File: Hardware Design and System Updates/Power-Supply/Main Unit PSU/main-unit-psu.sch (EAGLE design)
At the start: 12 parts, among them U1 BA033CC0FP-E2TO252-3_ROM, U2 BA033CC0FP-E2TO252-3_ROM

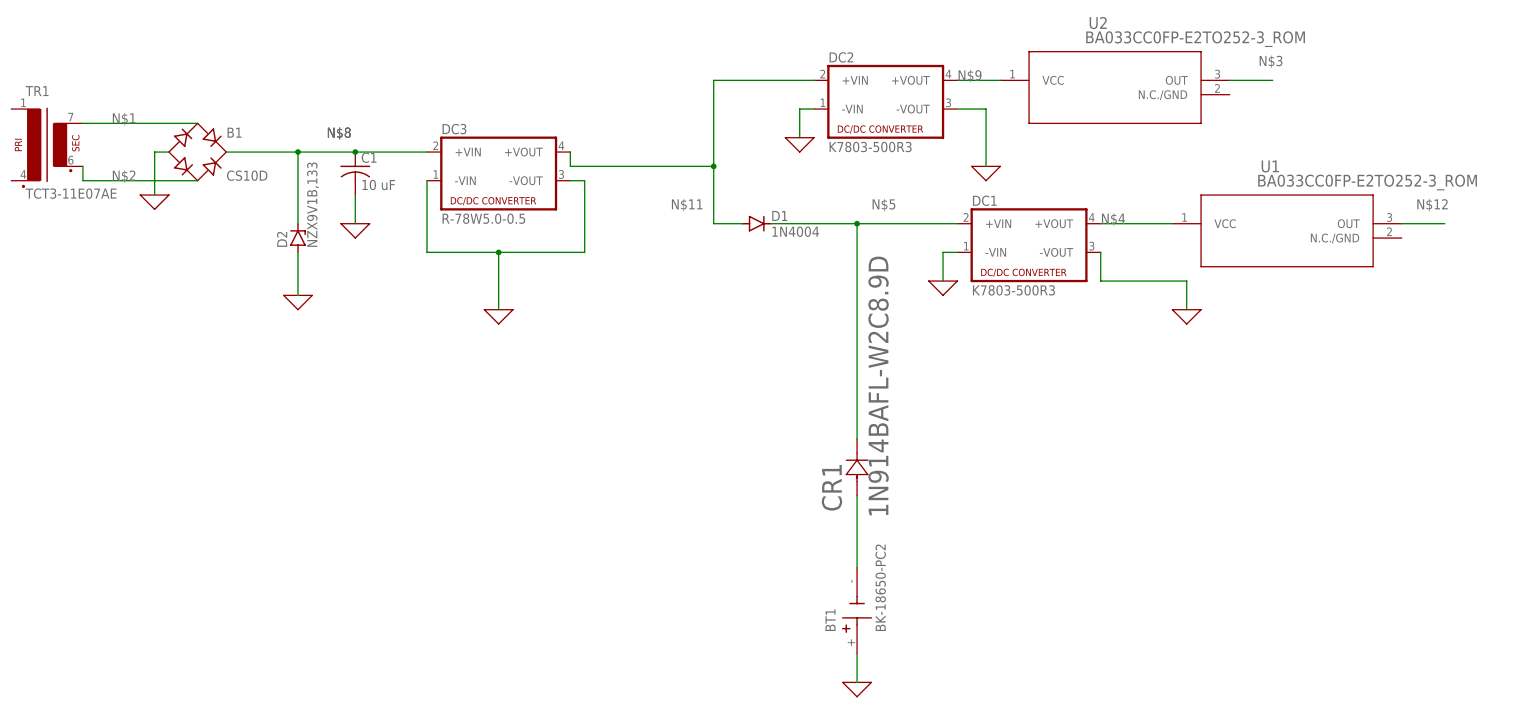
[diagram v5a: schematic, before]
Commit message: Fixed main and sub unit designs for voltage compat
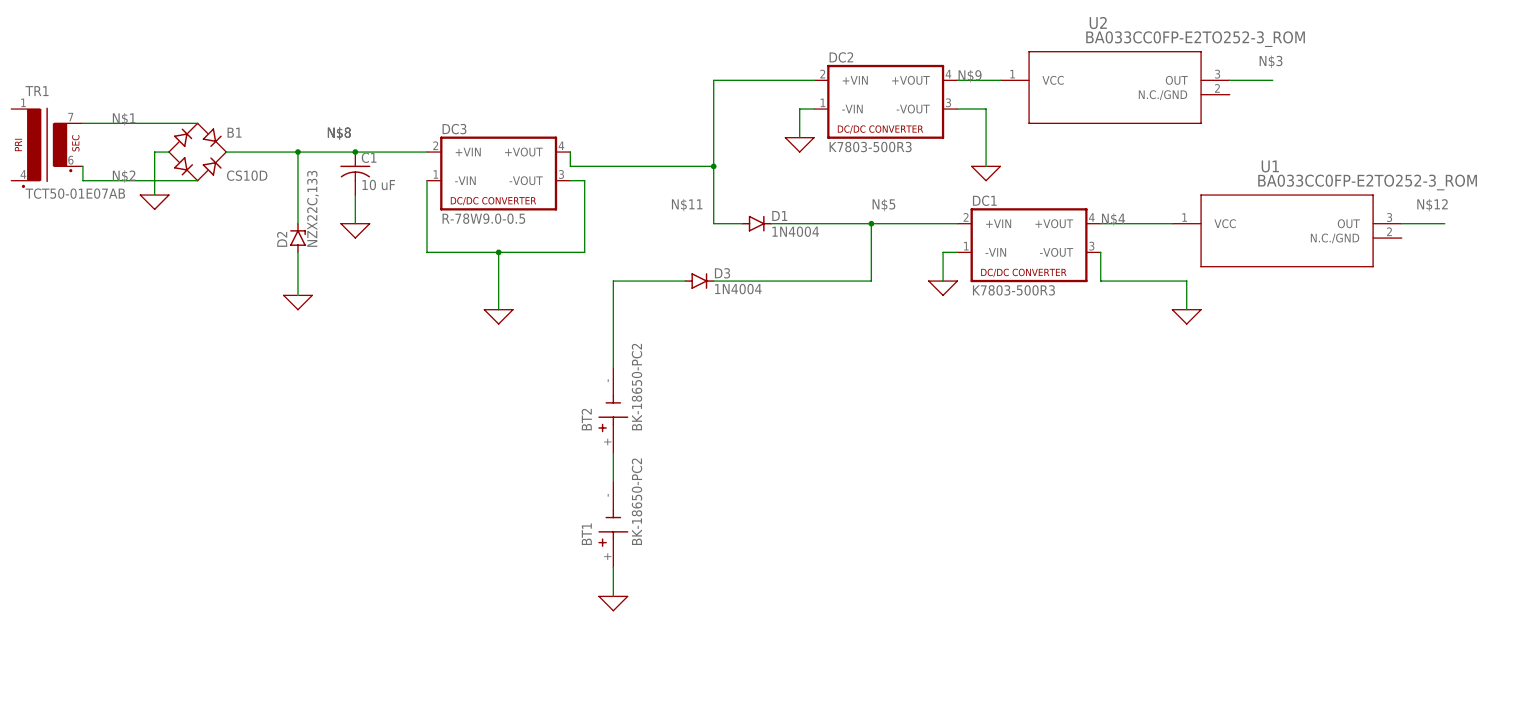
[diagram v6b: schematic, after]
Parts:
- removed CR1: 1N914BAFL-W2C8.9D, 2023-03-08_11-41-24_Library:1N914BAFL-W2C8.9D
- added BT2: BK-18650-PC2, BK-18650-PC2:BK-18650-PC2
- added D3: 1N4004, diode:1N4004
- D2: value NZX9V1B,133 -> NZX22C,133
- DC3: value R-78W5.0-0.5 -> R-78W9.0-0.5
- TR1: value TCT3-11E07AE -> TCT50-01E07AB
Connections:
- new net N$7: BT2.-, D3.A
- net N$5: now also D3.C; no longer CR1.1
- net N$6: now also BT2.+; no longer CR1.2
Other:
- moved on the sheet: BT1
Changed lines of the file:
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@@
 <part name="B1" library="rectifier" library_urn="urn:adsk.eagle:library:336" deviceset="B-DIL" device="" package3d_urn="urn:adsk.eagle:package:23868/1" value="CS10D"/>
 <part name="X_1" library="ngspice-simulation" library_urn="urn:adsk.eagle:library:527439" deviceset="GND" device=""/>
-<part name="D2" library="diode" library_urn="urn:adsk.eagle:library:210" deviceset="ZENER-DIODE" device="DO41Z10" package3d_urn="urn:adsk.eagle:package:43341/1" value="NZX9V1B,133"/>
+<part name="D2" library="diode" library_urn="urn:adsk.eagle:library:210" deviceset="ZENER-DIODE" device="DO41Z10" package3d_urn="urn:adsk.eagle:package:43341/1" value="NZX22C,133"/>
 <part name="X_2" library="ngspice-simulation" library_urn="urn:adsk.eagle:library:527439" deviceset="GND" device=""/>
 <part name="X_3" library="ngspice-simulation" library_urn="urn:adsk.eagle:library:527439" deviceset="GND" device=""/>
-<part name="TR1" library="trafo" library_urn="urn:adsk.eagle:library:394" deviceset="EE20-1" device="" package3d_urn="urn:adsk.eagle:package:28342/1" value="TCT3-11E07AE"/>
+<part name="TR1" library="trafo" library_urn="urn:adsk.eagle:library:394" deviceset="EE20-1" device="" package3d_urn="urn:adsk.eagle:package:28342/1" value="TCT50-01E07AB"/>
 <part name="DC1" library="dc-dc-converter" library_urn="urn:adsk.eagle:library:208" deviceset="NME" device="" package3d_urn="urn:adsk.eagle:package:12313/1" value="K7803-500R3"/>
 <part name="X_4" library="ngspice-simulation" library_urn="urn:adsk.eagle:library:527439" deviceset="GND" device=""/>
 <part name="DC2" library="dc-dc-converter" library_urn="urn:adsk.eagle:library:208" deviceset="NME" device="" package3d_urn="urn:adsk.eagle:package:12313/1" value="K7803-500R3"/>
 <part name="X_6" library="ngspice-simulation" library_urn="urn:adsk.eagle:library:527439" deviceset="GND" device=""/>
-<part name="CR1" library="2023-03-08_11-41-24_Library" deviceset="1N914B" device="AFL-W2C8.9D"/>
 <part name="BT1" library="BK-18650-PC2" deviceset="BK-18650-PC2" device=""/>
 <part name="X_5" library="ngspice-simulation" library_urn="urn:adsk.eagle:library:527439" deviceset="GND" device=""/>
-<part name="DC3" library="dc-dc-converter" library_urn="urn:adsk.eagle:library:208" deviceset="NME" device="" package3d_urn="urn:adsk.eagle:package:12313/1" value="R-78W5.0-0.5"/>
+<part name="DC3" library="dc-dc-converter" library_urn="urn:adsk.eagle:library:208" deviceset="NME" device="" package3d_urn="urn:adsk.eagle:package:12313/1" value="R-78W9.0-0.5"/>
 <part name="X_7" library="ngspice-simulation" library_urn="urn:adsk.eagle:library:527439" deviceset="GND" device=""/>
 <part name="U1" library="2023-03-08_12-17-23_Library" deviceset="BA033CC0FP-E2" device="TO252-3_ROM"/>
@@
 <part name="X_9" library="ngspice-simulation" library_urn="urn:adsk.eagle:library:527439" deviceset="GND" device=""/>
 <part name="U2" library="2023-03-08_12-17-23_Library" deviceset="BA033CC0FP-E2" device="TO252-3_ROM"/>
+<part name="BT2" library="BK-18650-PC2" deviceset="BK-18650-PC2" device=""/>
+<part name="D3" library="diode" library_urn="urn:adsk.eagle:library:210" deviceset="1N4004" device="" package3d_urn="urn:adsk.eagle:package:43336/1"/>
 </parts>
 <sheets>
@@
 </instance>
 <instance part="X_6" gate="G$1" x="83.82" y="71.12" smashed="yes"/>
-<instance part="CR1" gate="A" x="93.98" y="7.62" smashed="yes" rot="R90">
-<attribute name="VALUE" x="99.5299" y="3.7369" size="3.48" layer="96" ratio="10" rot="R90"/>
-<attribute name="NAME" x="91.2749" y="4.8052" size="3.48" layer="95" ratio="10" rot="R90"/>
-</instance>
-<instance part="BT1" gate="G$1" x="93.98" y="-12.7" smashed="yes" rot="R90">
-<attribute name="NAME" x="90.17" y="-16.51" size="1.778" layer="95" rot="R90"/>
-<attribute name="VALUE" x="99.06" y="-16.51" size="1.778" layer="96" rot="R90"/>
-</instance>
-<instance part="X_5" gate="G$1" x="93.98" y="-25.4" smashed="yes"/>
+<instance part="BT1" gate="G$1" x="50.8" y="2.54" smashed="yes" rot="R90">
+<attribute name="NAME" x="46.99" y="-1.27" size="1.778" layer="95" rot="R90"/>
+<attribute name="VALUE" x="55.88" y="-1.27" size="1.778" layer="96" rot="R90"/>
+</instance>
+<instance part="X_5" gate="G$1" x="50.8" y="-10.16" smashed="yes"/>
 <instance part="DC3" gate="G$1" x="30.48" y="66.04" smashed="yes">
 <attribute name="NAME" x="20.32" y="71.755" size="1.778" layer="95"/>
@@
 <attribute name="VALUE" x="134.3352" y="87.8586" size="2.083" layer="96" ratio="6"/>
 </instance>
+<instance part="BT2" gate="G$1" x="50.8" y="22.86" smashed="yes" rot="R90">
+<attribute name="NAME" x="46.99" y="19.05" size="1.778" layer="95" rot="R90"/>
+<attribute name="VALUE" x="55.88" y="19.05" size="1.778" layer="96" rot="R90"/>
+</instance>
+<instance part="D3" gate="1" x="66.04" y="45.72" smashed="yes">
+<attribute name="NAME" x="68.58" y="46.2026" size="1.778" layer="95"/>
+<attribute name="VALUE" x="68.58" y="43.4086" size="1.778" layer="96"/>
+</instance>
 </instances>
 <busses>
@@
 <pinref part="X_5" gate="G$1" pin="0"/>
 <pinref part="BT1" gate="G$1" pin="+"/>
-<wire x1="93.98" y1="-25.4" x2="93.98" y2="-20.32" width="0.1524" layer="91"/>
+<wire x1="50.8" y1="-10.16" x2="50.8" y2="-5.08" width="0.1524" layer="91"/>
 </segment>
 <segment>
@@
 <segment>
 <pinref part="D1" gate="1" pin="C"/>
-<wire x1="78.74" y1="55.88" x2="93.98" y2="55.88" width="0.1524" layer="91"/>
 <pinref part="DC1" gate="G$1" pin="+VIN"/>
-<wire x1="93.98" y1="55.88" x2="111.76" y2="55.88" width="0.1524" layer="91"/>
-<junction x="93.98" y="55.88"/>
+<wire x1="78.74" y1="55.88" x2="96.52" y2="55.88" width="0.1524" layer="91"/>
 <label x="96.52" y="58.42" size="1.778" layer="95"/>
-<pinref part="CR1" gate="A" pin="1"/>
-<wire x1="93.98" y1="17.78" x2="93.98" y2="55.88" width="0.1524" layer="91"/>
+<wire x1="96.52" y1="55.88" x2="111.76" y2="55.88" width="0.1524" layer="91"/>
+<wire x1="68.58" y1="45.72" x2="96.52" y2="45.72" width="0.1524" layer="91"/>
+<wire x1="96.52" y1="45.72" x2="96.52" y2="55.88" width="0.1524" layer="91"/>
+<junction x="96.52" y="55.88"/>
+<pinref part="D3" gate="1" pin="C"/>
 </segment>
 </net>
@@
 <net name="N$6" class="0">
 <segment>
+<pinref part="BT2" gate="G$1" pin="+"/>
 <pinref part="BT1" gate="G$1" pin="-"/>
-<pinref part="CR1" gate="A" pin="2"/>
-<wire x1="93.98" y1="-5.08" x2="93.98" y2="7.62" width="0.1524" layer="91"/>
-</segment>
-</net>
+<wire x1="50.8" y1="10.16" x2="50.8" y2="15.24" width="0.1524" layer="91"/>
+</segment>
+</net>
+<net name="N$7" class="0">
+<segment>
+<pinref part="BT2" gate="G$1" pin="-"/>
+<wire x1="50.8" y1="30.48" x2="50.8" y2="45.72" width="0.1524" layer="91"/>
+<wire x1="63.5" y1="45.72" x2="50.8" y2="45.72" width="0.1524" layer="91"/>
+<pinref part="D3" gate="1" pin="A"/>
+</segment>
+</net>

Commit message: Fixed label and added total to BOM
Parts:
- B1: value CS10D -> KMB23S
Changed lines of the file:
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@@
 <part name="D1" library="diode" library_urn="urn:adsk.eagle:library:210" deviceset="1N4004" device="" package3d_urn="urn:adsk.eagle:package:43336/1"/>
 <part name="C1" library="rcl" library_urn="urn:adsk.eagle:library:334" deviceset="C-US" device="050-024X044" package3d_urn="urn:adsk.eagle:package:23643/1" value="10 uF"/>
-<part name="B1" library="rectifier" library_urn="urn:adsk.eagle:library:336" deviceset="B-DIL" device="" package3d_urn="urn:adsk.eagle:package:23868/1" value="CS10D"/>
+<part name="B1" library="rectifier" library_urn="urn:adsk.eagle:library:336" deviceset="B-DIL" device="" package3d_urn="urn:adsk.eagle:package:23868/1" value="KMB23S"/>
 <part name="X_1" library="ngspice-simulation" library_urn="urn:adsk.eagle:library:527439" deviceset="GND" device=""/>
 <part name="D2" library="diode" library_urn="urn:adsk.eagle:library:210" deviceset="ZENER-DIODE" device="DO41Z10" package3d_urn="urn:adsk.eagle:package:43341/1" value="NZX22C,133"/>
